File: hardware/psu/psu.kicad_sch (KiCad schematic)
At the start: 43 parts, among them J1 Conn_01x02, J3 Conn_01x02, J4 Conn_01x06, T1 AS-1T175

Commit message: ps board
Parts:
- added C11, C12: 10u 250V, Capacitor_THT:CP_Radial_D10.0mm_P5.00mm, symbol Device:C_Polarized_Small_US
- added D11, D12: 1N4007, Diode_THT:D_DO-41_SOD81_P10.16mm_Horizontal, symbol Diode:1N4007
- added D13: 1N5386BG, Diode_THT:D_DO-41_SOD81_P12.70mm_Horizontal, symbol Device:D_Zener
- added H1, H2, H3, H4: MountingHole, MountingHole:MountingHole_4.3mm_M4, symbol Mechanical:MountingHole
- added J6: Conn_01x05, Connector_Molex:Molex_KK-396_A-41791-0005_1x05_P3.96mm_Vertical, symbol Connector_Generic:Conn_01x05
- added J7: Conn_01x08, Connector_Molex:Molex_KK-396_A-41791-0008_1x08_P3.96mm_Vertical, symbol Connector_Generic:Conn_01x08
- added J8: Conn_01x03, Connector_Molex:Molex_KK-396_A-41791-0003_1x03_P3.96mm_Vertical, symbol Connector_Generic:Conn_01x03
- added JP1, JP2: Jumper_2_Open, Connector_PinHeader_2.54mm:PinHeader_1x02_P2.54mm_Vertical, symbol Jumper:Jumper_2_Open
- added R4: 100 ohm 1/2W, Resistor_THT:R_Axial_DIN0309_L9.0mm_D3.2mm_P12.70mm_Horizontal, symbol Device:R_US
- added R5: 2.6k ohm 2W, Resistor_THT:R_Axial_DIN0207_L6.3mm_D2.5mm_P10.16mm_Horizontal, symbol Device:R_US
- C1, C10, C2, C3, C4, C5, C6, C7, C8, C9: footprint (none) -> Capacitor_THT:CP_Radial_D13.0mm_P7.50mm
- C13: renamed from C?; footprint (none) -> Capacitor_THT:CP_Radial_D5.0mm_P2.00mm; CatNo (none) -> 732-8625-1-ND
- C14, C15: renamed from C?; footprint (none) -> Capacitor_THT:CP_Radial_D5.0mm_P2.00mm; CatNo (none) -> 732-8851-1-ND
- D14: renamed from D?; footprint (none) -> Diode_THT:Diode_Bridge_15.1x15.1x6.3mm_P10.9mm
- D15, D16: renamed from D?; footprint (none) -> LED_THT:LED_D3.0mm
- F1: renamed from F?; footprint (none) -> HBH_fuse_holder:HBH-I-R
- J1: footprint (none) -> Connector_PinHeader_2.54mm:PinHeader_1x02_P2.54mm_Vertical
- J2: renamed from J?; footprint (none) -> GSP1_power_entry:GSP1.8101.1
- J3: footprint (none) -> Connector_Molex:Molex_KK-396_A-41791-0002_1x02_P3.96mm_Vertical
- J4: footprint (none) -> Connector_Molex:Molex_KK-396_A-41791-0006_1x06_P3.96mm_Vertical
- J5: renamed from J?; footprint (none) -> Connector_Molex:Molex_KK-396_A-41791-0003_1x03_P3.96mm_Vertical
- J9: renamed from J?; footprint (none) -> Connector_Molex:Molex_KK-254_AE-6410-04A_1x04_P2.54mm_Vertical
- NE1: renamed from NE?; footprint (none) -> LED_THT:LED_D1.8mm_W1.8mm_H2.4mm_Horizontal_O3.81mm_Z4.9mm
- R1: value 100 -> 100 ohm 1/2W; footprint (none) -> Resistor_THT:R_Axial_DIN0309_L9.0mm_D3.2mm_P12.70mm_Horizontal; CatNo (none) -> CF12JT100RTR-ND
- R2: value R_US -> 100 ohm 1/2W; footprint (none) -> Resistor_THT:R_Axial_DIN0309_L9.0mm_D3.2mm_P12.70mm_Horizontal; CatNo (none) -> CF12JT100RTR-ND
- R3: renamed from R?; footprint (none) -> Resistor_THT:R_Axial_DIN0309_L9.0mm_D3.2mm_P12.70mm_Horizontal
- R6: renamed from R?; value R_US -> 1.2k; footprint (none) -> Resistor_THT:R_Axial_DIN0207_L6.3mm_D2.5mm_P10.16mm_Horizontal
- R7: renamed from R?; value R_US -> 650; footprint (none) -> Resistor_THT:R_Axial_DIN0207_L6.3mm_D2.5mm_P10.16mm_Horizontal
- SW1: renamed from SW?; footprint (none) -> Switch_8GA:8GA1016-Z
- gave numbers to parts that had none: 2
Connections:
- net -1400: now also C10.2, D10.2 (A); no longer C3.2, D1.2 (A), T1.7 (H1B)
- net 0V: now also C3.1, D1.1 (K), T1.7 (H1B), J7.2 (Pin_2), J7.4 (Pin_4), JP1.2 (B); no longer C10.1, D10.1 (K)
- net GND: now also D14.2 (-), T1.4 (SH), J6.5 (Pin_5), J8.3 (Pin_3), JP1.1 (A), JP2.2 (B); no longer D14.4, T1.13 (F2B)
- net SW_ACL: now reaches J5.1 (Pin_1), NE1.1, SW1.2 (B), T1.1 (P1A)
- net SW_ACL: now also J6.1 (Pin_1)
- net 6.3_1A: now reaches J1.1 (Pin_1), T1.10 (F1A)
- net 6.3_1A: now also J7.5 (Pin_5), J7.6 (Pin_6)
- net 6.3_1B: now reaches J1.2 (Pin_2), T1.11 (F1B)
- net at C13.1, U1.1 (VI): now also D14.1 (+); no longer D14.3, T1.12 (F2A)
- net ACN: now reaches J2.3 (Pin_3), J5.2 (Pin_2), R3.1, T1.2 (P1B)
- net ACN: now also J6.2 (Pin_2)
- net 115_A: now reaches T1.3 (P2A)
- net 115_A: now also C12.2, D11.2 (A), D13.2 (A), J6.3 (Pin_3), J8.2 (Pin_2), JP2.1 (A)
- net 175_1A: now reaches R1.1, T1.6 (H1A)
- net 175_1A: now also J7.1 (Pin_1)
- net 175_2A: now reaches R2.1, T1.8 (H2A)
- net 175_2A: now also J7.3 (Pin_3)
- net at C1.2: now also C5.1, D1.2 (A), D3.1 (K); no longer R1.2
- new net: C12.1, D12.1 (K), R5.1
- new net: C11.1, D11.1 (K), D12.2 (A)
- new net: C10.1, C8.2, D8.2 (A), D9.1 (K)
- new net: C9.2, D10.1 (K), D9.2 (A)
- new net: C5.2, C7.1, D5.2 (A), D6.1 (K)
- new net: C6.2, C8.1, D6.2 (A), D7.1 (K)
- new net: C3.2, C6.1, D3.2 (A), D5.1 (K)
- new net: D13.1 (K), J8.1 (Pin_1), R5.2
- new net: C1.1, R1.2
- new net: C11.2, R4.2
- new net: C7.2, C9.1, D7.2 (A), D8.1 (K)
- new net 115_B: J6.4 (Pin_4), R4.1, T1.4 (SH)
- new net 6.3_2A: D14.3, J7.7 (Pin_7), T1.12 (F2A)
- new net 6.3_2B: D14.4, J7.8 (Pin_8), T1.13 (F2B)
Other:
- note added: "+180V 15mA for Nixie/neon Switched AC for other transfomers"
- note added: "180V zener"
- note added: "360V B+ to deflection amp"
- note added: "Aux. 180V out (nixie, neon etc)"
- note added: "CRT FIL 6.3V"
- note added: "HV OUT to CRT"
- note added: "Negative 8-stage Cockroft-Walton multipler"
- note added: "Switched AC OUT (filament transfomer)"
- note added: "Transfomer mounted remotely with connectors"
- note added: "voltage doubler"
- note removed: "AC OUT (filament transfomer)"
- note removed: "Antek AS-1T175 has 2x115V, 2x6.3V and 2x175V windings +360V: doubler on 175V -1400V: 8x Cockroft-Walton on 175V 6.3V for CRT filament (other unused or for 6SN7 option)"
- note removed: "CRT FIL"
- note removed: "to CRT"
- note removed: "to Deflection amp"
- moved on the sheet: C1, C10, C13, C14, C15, C2, C3, C4, C5, C6, C7, C8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

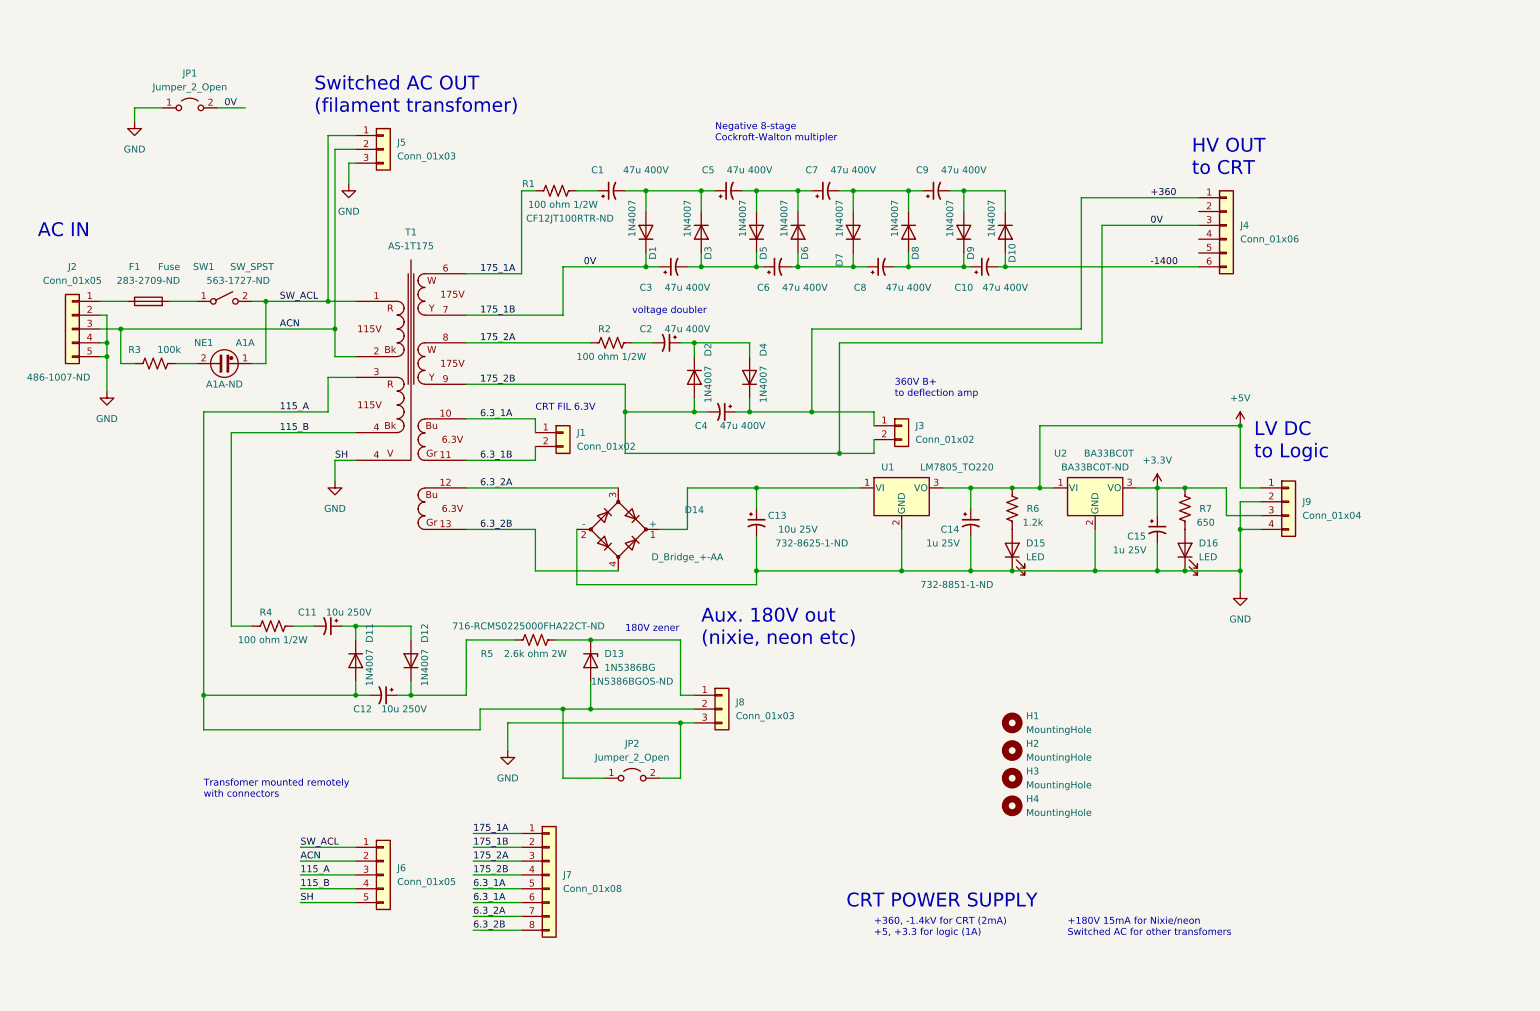
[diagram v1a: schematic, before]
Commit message: rework power supply, still needs footprint/placement work
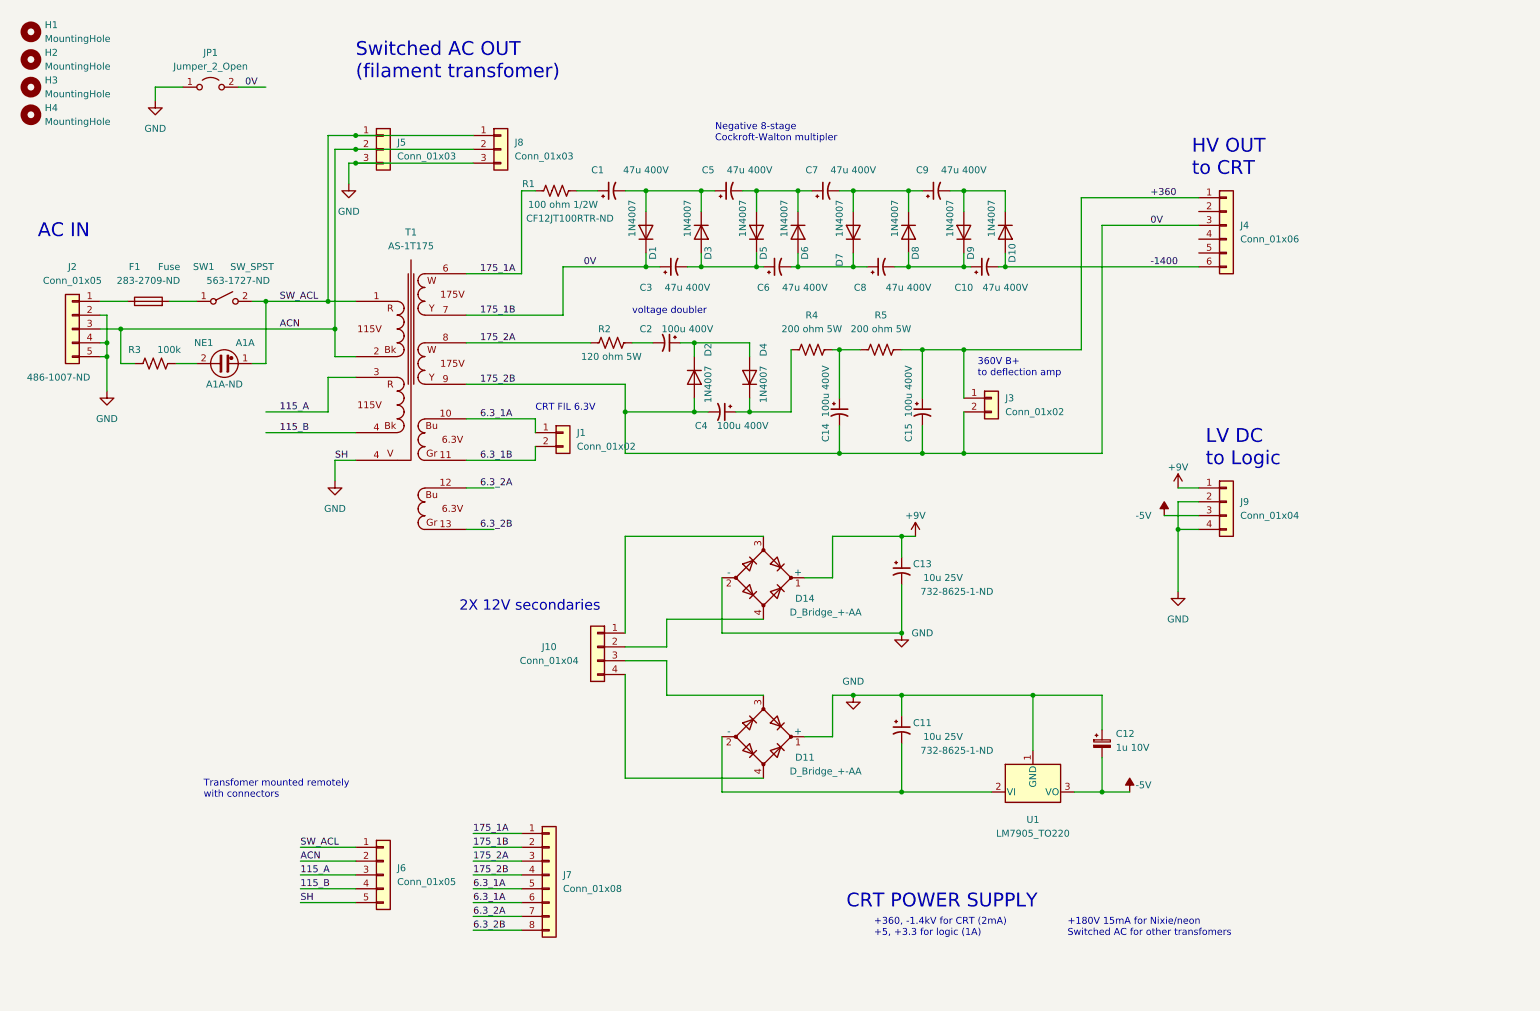
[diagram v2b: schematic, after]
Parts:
- removed C12: 10u 250V, Capacitor_THT:CP_Radial_D10.0mm_P5.00mm, symbol Device:C_Polarized_Small_US
- removed D11, D12: 1N4007, Diode_THT:D_DO-41_SOD81_P10.16mm_Horizontal, symbol Diode:1N4007
- removed D13: 1N5386BG, Diode_THT:D_DO-41_SOD81_P12.70mm_Horizontal, symbol Device:D_Zener
- removed D15, D16: LED, LED_THT:LED_D3.0mm, symbol Device:LED
- removed JP2: Jumper_2_Open, Connector_PinHeader_2.54mm:PinHeader_1x02_P2.54mm_Vertical, symbol Jumper:Jumper_2_Open
- removed R6: 1.2k, Resistor_THT:R_Axial_DIN0207_L6.3mm_D2.5mm_P10.16mm_Horizontal, symbol Device:R_US
- removed R7: 650, Resistor_THT:R_Axial_DIN0207_L6.3mm_D2.5mm_P10.16mm_Horizontal, symbol Device:R_US
- removed U1: LM7805_TO220, Package_TO_SOT_THT:TO-220-3_Vertical, symbol Regulator_Linear:LM7805_TO220
- removed U2: BA33BC0T, Package_TO_SOT_THT:TO-220-3_Vertical, symbol Regulator_Linear:LM7805_TO220
- added C12: 1u 10V, Capacitor_THT:CP_Radial_D5.0mm_P2.00mm, symbol Device:C_Polarized_Small
- added D11: D_Bridge_+-AA, Diode_THT:Diode_Bridge_15.1x15.1x6.3mm_P10.9mm, symbol Device:D_Bridge_+-AA
- added J10: Conn_01x04, Connector_Molex:Molex_KK-254_AE-6410-04A_1x04_P2.54mm_Vertical, symbol Connector_Generic:Conn_01x04
- added U1: LM7905_TO220, Package_TO_SOT_THT:TO-220-3_Vertical, symbol Regulator_Linear:LM7905_TO220
- C11: value 10u 250V -> 10u 25V; footprint Capacitor_THT:CP_Radial_D10.0mm_P5.00mm -> Capacitor_THT:CP_Radial_D5.0mm_P2.00mm; CatNo 493-12846-1-ND -> 732-8625-1-ND
- C14, C15: value 1u 25V -> 100u 400V; footprint Capacitor_THT:CP_Radial_D5.0mm_P2.00mm -> Capacitor_THT:CP_Radial_D22.0mm_P10.00mm_SnapIn; CatNo 732-8851-1-ND -> (none)
- C2, C4: value 47u 400V -> 100u 400V; footprint Capacitor_THT:CP_Radial_D13.0mm_P7.50mm -> Capacitor_THT:CP_Radial_D22.0mm_P10.00mm_SnapIn
- R2: value 100 ohm 1/2W -> 120 ohm 5W; footprint Resistor_THT:R_Axial_DIN0309_L9.0mm_D3.2mm_P12.70mm_Horizontal -> Resistor_THT:R_Axial_Power_L25.0mm_W6.4mm_P27.94mm; CatNo CF12JT100RTR-ND -> (none)
- R4: value 100 ohm 1/2W -> 200 ohm 5W; footprint Resistor_THT:R_Axial_DIN0309_L9.0mm_D3.2mm_P12.70mm_Horizontal -> Resistor_THT:R_Axial_Power_L25.0mm_W6.4mm_P27.94mm; CatNo CF12JT100RTR-ND -> (none)
- R5: value 2.6k ohm 2W -> 200 ohm 5W; footprint Resistor_THT:R_Axial_DIN0207_L6.3mm_D2.5mm_P10.16mm_Horizontal -> Resistor_THT:R_Axial_Power_L25.0mm_W6.4mm_P27.94mm; CatNo 716-RCMS0225000FHA22CT-ND -> (none)
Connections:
- net +360: now also C15.1, R5.2; no longer C4.1, D4.1 (K)
- net 0V: now also C14.2, C15.2
- net 115_A: no longer J8.2 (Pin_2)
- net 115_B: no longer R4.1
- net 6.3_2A: no longer D14.3
- net 6.3_2B: no longer D14.4
- net ACN: now also J8.2 (Pin_2)
- net GND: now also C11.1, C12.1, D11.1 (+), U1.1 (GND); no longer C14.2, C15.2
- net SW_ACL: now also J8.1 (Pin_1)
- net at R5.1: now also C14.1, R4.2
- net at C11.2: now also D11.2 (-), U1.2 (VI); no longer R4.2
- net +9V: now reaches C13.1, D14.1 (+)
- net +9V: now also J9.1 (Pin_1)
- net +3.3V renamed -5V
- net -5V: now also C12.2, U1.3 (VO); no longer C15.1
- removed net +5V: C14.1, J9.1 (Pin_1)
- new net: C4.1, D4.1 (K), R4.1
- new net: D11.3, J10.3 (Pin_3)
- new net: D11.4, J10.4 (Pin_4)
- new net: D14.3, J10.1 (Pin_1)
- new net: D14.4, J10.2 (Pin_2)
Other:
- note added: "2X 12V secondaries"
- note removed: "180V zener"
- note removed: "Aux. 180V out (nixie, neon etc)"
- moved on the sheet: C13, D14, H1, H2, H3, H4, J3, J9, JP1

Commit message: Add some stuff to PSU
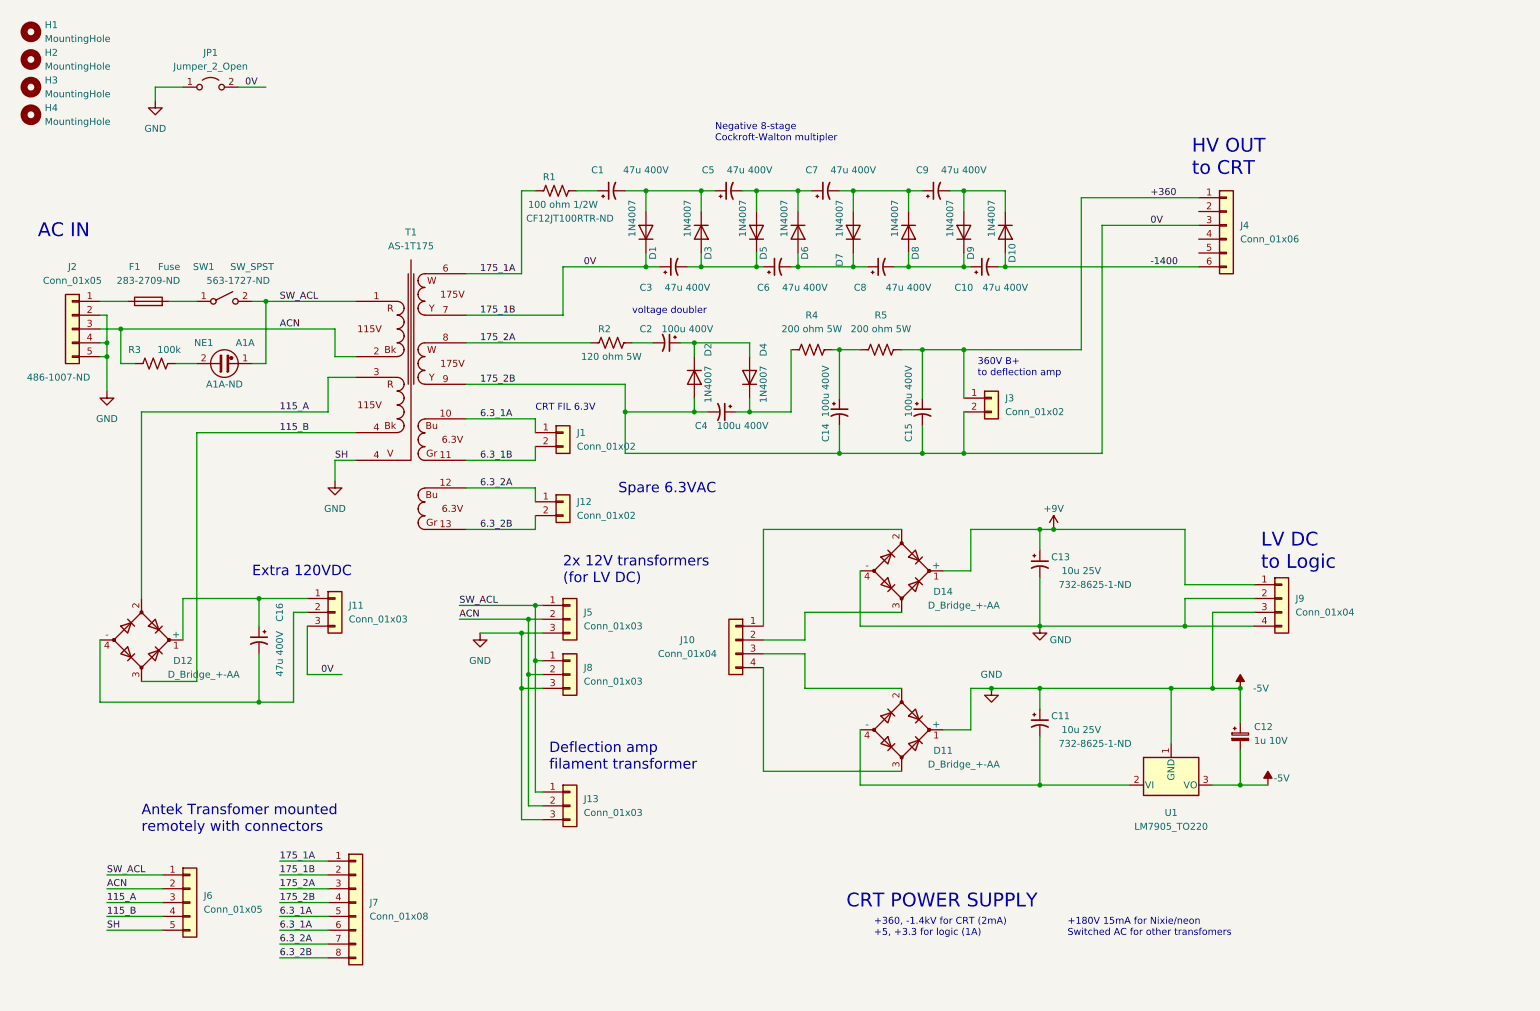
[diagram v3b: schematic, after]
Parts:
- added C16: 47u 400V, Capacitor_THT:CP_Radial_D13.0mm_P7.50mm, symbol Device:C_Polarized_Small_US
- added D12: D_Bridge_+-AA, Diode_THT:Diode_Bridge_19.0x3.5x10.0mm_P5.0mm, symbol Device:D_Bridge_+AA-
- added J11, J13: Conn_01x03, Connector_Molex:Molex_KK-396_A-41791-0003_1x03_P3.96mm_Vertical, symbol Connector_Generic:Conn_01x03
- added J12: Conn_01x02, Connector_PinHeader_2.54mm:PinHeader_1x02_P2.54mm_Vertical, symbol Connector_Generic:Conn_01x02
- D11, D14: footprint Diode_THT:Diode_Bridge_15.1x15.1x6.3mm_P10.9mm -> Diode_THT:Diode_Bridge_19.0x3.5x10.0mm_P5.0mm; symbol Device:D_Bridge_+-AA -> Device:D_Bridge_+AA-; CatNo (none) -> GBU4G-BPMS-ND
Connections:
- net -5V: now also C11.1, C12.1, C13.2, D11.1 (+), D14.4 (-), J2.2 (Pin_2), J2.4 (Pin_4), J2.5 (Pin_5), J5.3 (Pin_3), J6.5 (Pin_5), J8.3 (Pin_3), J9.2 (Pin_2), J9.4 (Pin_4), JP1.1 (A), T1.4 (SH), U1.1 (GND), J13.3 (Pin_3)
- net 0V: now also J11.3 (Pin_3)
- net 115_A: now also D12.2
- net 115_B: now also D12.3
- net 6.3_2A: now also J12.1 (Pin_1)
- net 6.3_2B: now also J12.2 (Pin_2)
- net ACN: now also J13.2 (Pin_2)
- net SW_ACL: now also J13.1 (Pin_1)
- net at C11.2, U1.2 (VI): now also D11.4 (-); no longer D11.2 (-)
- net at J10.3 (Pin_3): now also D11.2; no longer D11.3
- net at J10.4 (Pin_4): now also D11.3; no longer D11.4
- net at J10.1 (Pin_1): now also D14.2; no longer D14.3
- net at J10.2 (Pin_2): now also D14.3; no longer D14.4
- removed net GND: C11.1, C12.1, C13.2, D11.1 (+), D14.2 (-), J2.2 (Pin_2), J2.4 (Pin_4), J2.5 (Pin_5), J5.3 (Pin_3), J6.5 (Pin_5), J8.3 (Pin_3), J9.2 (Pin_2), J9.4 (Pin_4), JP1.1 (A), T1.4 (SH), U1.1 (GND)
- new net: C16.1, D12.1 (+), J11.1 (Pin_1)
- new net: C16.2, D12.4 (-), J11.2 (Pin_2)
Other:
- note added: "2x 12V transformers (for LV DC)"
- note added: "Antek Transfomer mounted remotely with connectors"
- note added: "Deflection amp filament transformer"
- note added: "Extra 120VDC"
- note added: "Spare 6.3VAC"
- note removed: "2X 12V secondaries"
- note removed: "Switched AC OUT (filament transfomer)"
- note removed: "Transfomer mounted remotely with connectors"
- moved on the sheet: C11, C12, C13, D11, D14, J10, J5, J6, J7, J8, J9, U1
